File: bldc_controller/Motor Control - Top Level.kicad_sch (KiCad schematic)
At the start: 10 parts, among them U8 DRV8353FS

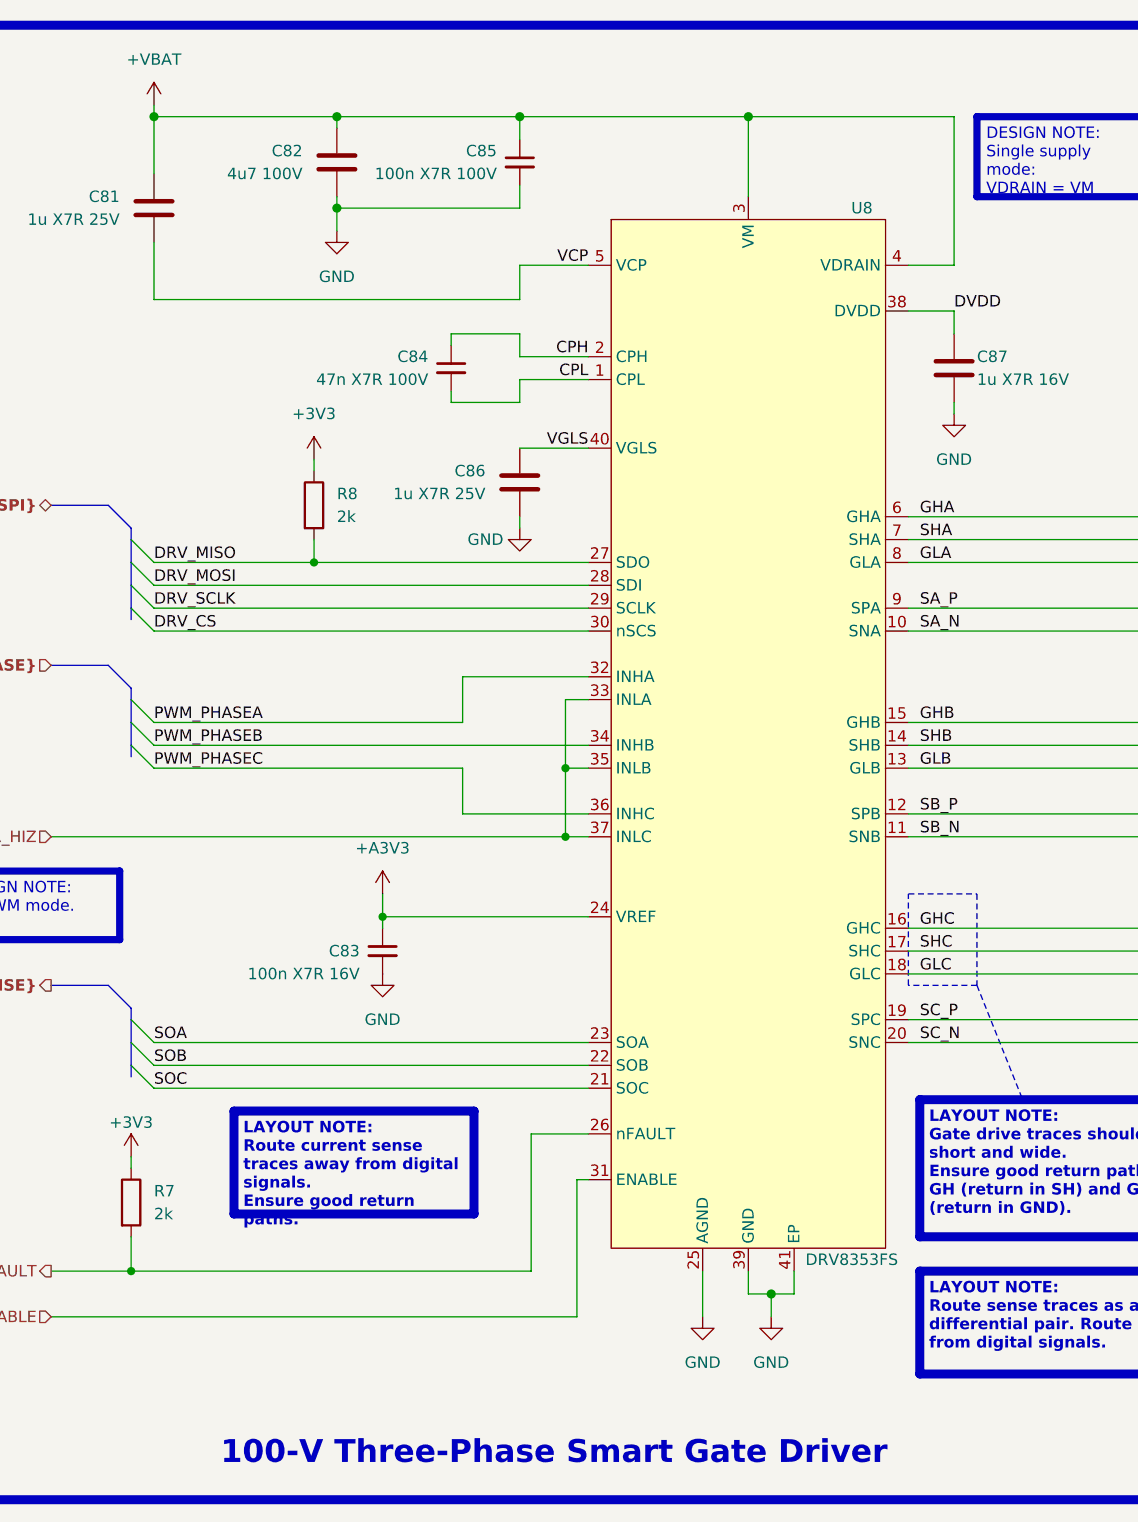
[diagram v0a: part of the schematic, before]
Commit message: schematic is complete. Replaced 5V buck and added pi filters.
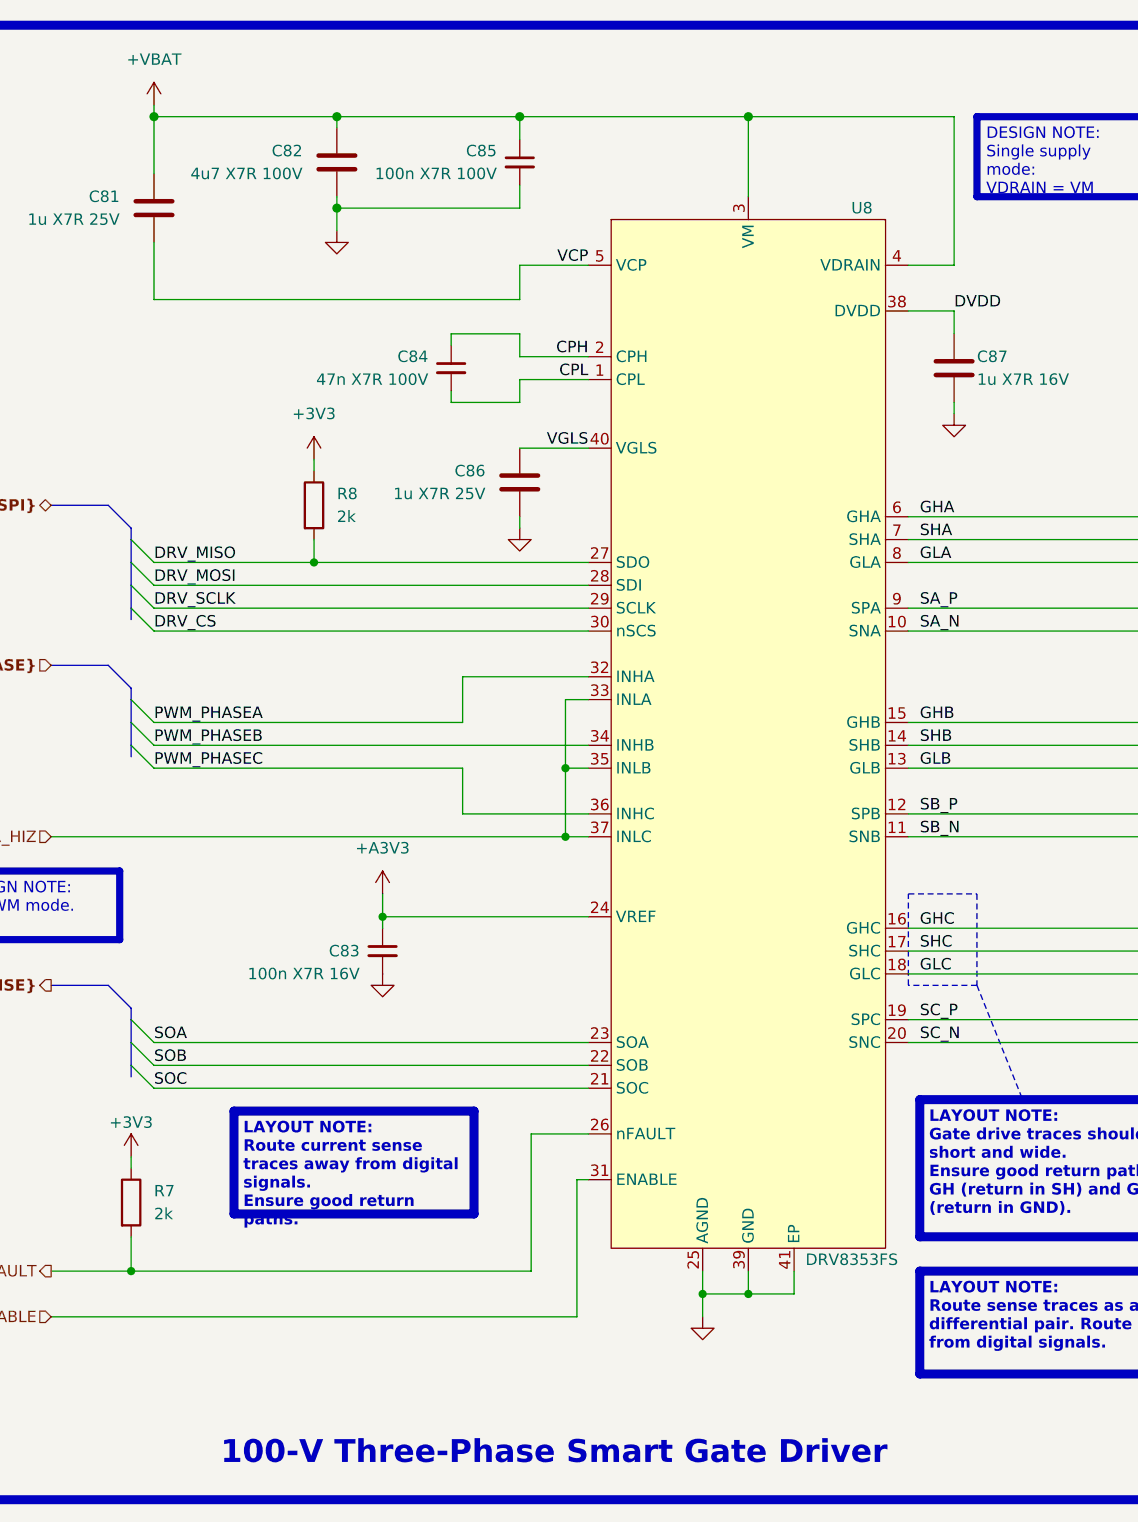
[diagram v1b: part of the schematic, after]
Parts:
- C82: value 4u7 100V -> 4u7 X7R 100V
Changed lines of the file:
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@@
   (junction (at 125.73 68.58) (diameter 1.016) (color 0 0 0 0)
   )
-  (junction (at 173.99 199.39) (diameter 1.016) (color 0 0 0 0)
+  (junction (at 171.45 199.39) (diameter 0) (color 0 0 0 0)
   )
   (junction (at 105.41 68.58) (diameter 1.016) (color 0 0 0 0)
@@
   (junction (at 123.19 118.11) (diameter 0) (color 0 0 0 0)
   )
+  (junction (at 166.37 199.39) (diameter 0) (color 0 0 0 0)
+  )
   (junction (at 130.81 157.48) (diameter 0) (color 0 0 0 0)
   )
@@
     (stroke (width 0) (type default))
   )
-  (wire (pts (xy 173.99 201.93) (xy 173.99 199.39))
+  (wire (pts (xy 166.37 201.93) (xy 166.37 199.39))
+    (stroke (width 0) (type default))
+  )
+  (wire (pts (xy 166.37 199.39) (xy 171.45 199.39))
     (stroke (width 0) (type default))
   )
@@
     (stroke (width 0) (type default))
   )
-  (wire (pts (xy 171.45 199.39) (xy 173.99 199.39))
-    (stroke (width 0) (type default))
-  )
   (wire (pts (xy 153.67 146.05) (xy 139.7 146.05))
     (stroke (width 0) (type default))
@@
     (stroke (width 0) (type default))
   )
-  (wire (pts (xy 166.37 196.85) (xy 166.37 201.93))
+  (wire (pts (xy 166.37 196.85) (xy 166.37 199.39))
     (stroke (width 0) (type default))
   )
@@
     (stroke (width 0) (type default))
   )
+  (wire (pts (xy 171.45 199.39) (xy 176.53 199.39))
+    (stroke (width 0) (type default))
+  )
   (bus (pts (xy 102.87 171.45) (xy 102.87 173.99))
     (stroke (width 0) (type default))
@@
   )
   (wire (pts (xy 146.05 97.79) (xy 153.67 97.79))
-    (stroke (width 0) (type default))
-  )
-  (wire (pts (xy 173.99 199.39) (xy 176.53 199.39))
     (stroke (width 0) (type default))
   )
@@
     )
     (property "Value" "GND" (at 142.24 115.57 0)
-      (effects (font (size 1.27 1.27)))
+      (effects (font (size 1.27 1.27)) hide)
     )
     (property "Footprint" "" (at 146.05 114.3 0)
@@
     )
   )
-  (symbol (lib_id "power:GND") (at 173.99 201.93 0) (unit 1)
+  (symbol (lib_id "power:GND") (at 166.37 201.93 0) (unit 1)
     (in_bom yes) (on_board yes) (dnp no) (fields_autoplaced)
-    (property "Reference" "#PWR033" (at 173.99 208.28 0)
-      (effects (font (size 1.27 1.27)) hide)
-    )
-    (property "Value" "GND" (at 173.99 207.01 0)
-      (effects (font (size 1.27 1.27)))
-    )
-    (property "Footprint" "" (at 173.99 201.93 0)
-      (effects (font (size 1.27 1.27)) hide)
-    )
-    (property "Datasheet" "" (at 173.99 201.93 0)
+    (property "Reference" "#PWR033" (at 166.37 208.28 0)
+      (effects (font (size 1.27 1.27)) hide)
+    )
+    (property "Value" "GND" (at 166.37 207.01 0)
+      (effects (font (size 1.27 1.27)) hide)
+    )
+    (property "Footprint" "" (at 166.37 201.93 0)
+      (effects (font (size 1.27 1.27)) hide)
+    )
+    (property "Datasheet" "" (at 166.37 201.93 0)
       (effects (font (size 1.27 1.27)) hide)
     )
@@
     )
     (property "Value" "GND" (at 130.81 168.91 0)
-      (effects (font (size 1.27 1.27)))
+      (effects (font (size 1.27 1.27)) hide)
     )
     (property "Footprint" "" (at 130.81 163.83 0)
@@
       (effects (font (size 1.27 1.27)) (justify left))
     )
-    (property "Value" "4u7 100V" (at 121.92 74.93 0)
+    (property "Value" "4u7 X7R 100V" (at 121.92 74.93 0)
       (effects (font (size 1.27 1.27)) (justify left))
     )
@@
     )
     (property "Value" "GND" (at 194.31 106.68 0)
-      (effects (font (size 1.27 1.27)))
+      (effects (font (size 1.27 1.27)) hide)
     )
     (property "Footprint" "" (at 194.31 101.6 0)
@@
     )
     (property "Value" "GND" (at 125.73 86.36 0)
-      (effects (font (size 1.27 1.27)))
+      (effects (font (size 1.27 1.27)) hide)
     )
     (property "Footprint" "" (at 125.73 81.28 0)
@@
         )
       )
-    )
-  )
-  (symbol (lib_id "power:GND") (at 166.37 201.93 0) (unit 1)
-    (in_bom yes) (on_board yes) (dnp no) (fields_autoplaced)
-    (property "Reference" "#PWR032" (at 166.37 208.28 0)
-      (effects (font (size 1.27 1.27)) hide)
-    )
-    (property "Value" "GND" (at 166.37 207.01 0)
-      (effects (font (size 1.27 1.27)))
-    )
-    (property "Footprint" "" (at 166.37 201.93 0)
-      (effects (font (size 1.27 1.27)) hide)
-    )
-    (property "Datasheet" "" (at 166.37 201.93 0)
-      (effects (font (size 1.27 1.27)) hide)
-    )
-    (pin "1")
-    (instances
-      (project "bldc_controller"
-        (path "/0650c7a8-acba-429c-9f8e-eec0baf0bc1c/fede4c36-00cc-4d3d-b71c-5243ba232202/5bcbc7e4-0942-415e-ab04-e1cd42538fc3"
-          (reference "#PWR032") (unit 1)
-        )
-      )

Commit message: added assembly files
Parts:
- R7, R8: value 2k -> 2k 1%
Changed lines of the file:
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@@
       (effects (font (size 1.27 1.27)) (justify left))
     )
-    (property "Value" "2k" (at 105.41 190.5 0)
+    (property "Value" "2k 1%" (at 105.41 190.5 0)
       (effects (font (size 1.27 1.27)) (justify left))
     )
@@
       (effects (font (size 1.27 1.27)) (justify left))
     )
-    (property "Value" "2k" (at 125.73 113.03 0)
-      (effects (font (size 1.27 1.27)) (justify left))
-    )
+    (property "Value" "2k 1%" (at 125.73 113.03 0)
+      (effects (font (size 1.27 1.27)) (justify left))
+    )
